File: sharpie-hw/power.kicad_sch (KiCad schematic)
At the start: 11 parts, among them J1 USB_C_Receptacle, U1 TLV1117-33, U2 TLV75801PDBV

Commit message: sharpie-hw prototype 1: complete
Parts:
- removed J1: USB_C_Receptacle, symbol Connector:USB_C_Receptacle
- removed U1: TLV1117-33, symbol Regulator_Linear:TLV1117-33
- removed U2: TLV75801PDBV, Package_TO_SOT_SMD:SOT-23-5, symbol Regulator_Linear:TLV75801PDBV
- added C22, C23: 100n, symbol Device:C
- added C24: 1u X7R, symbol Device:C
- added C25, C26: 10u X7R, symbol Device:C
- added J3: USB_C_Receptacle_USB2.0_16P, symbol Connector:USB_C_Receptacle_USB2.0_16P
- added J6: Conn_01x02_MountingPin, symbol Connector_Generic_MountingPin:Conn_01x02_MountingPin
- added R12: 100k, symbol Device:R
- added U1: TPS7A2533, symbol sharpie-hw:TPS7A2533
- added U2: TPS7A2501, symbol sharpie-hw:TPS7A2501
- added U5: LS021B7DD02, symbol sharpie-hw:Sharp_LS021B7DD02
- added U7: AP3602A, symbol sharpie-hw:AP3602A
- C2: value 2.2u X7R -> 1u X7R
- C3: value 1u X7R -> 2.2u X7R
- R3: value 62k -> 1.62M
- R4: value 13k -> 1.02M
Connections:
- net +3.2V: now also C23.1, U2.1 (OUT), U5.9 (VDD1)
- net +3.3V: now also U1.1 (OUT)
- net +5V: now also C22.1, C26.1, U5.1 (VDD2), U7.1 (Vout); no longer C1.1, C2.1
- net D+: now also J3.A6 (D+), J3.B6 (D+)
- net D-: now also J3.A7 (D-), J3.B7 (D-)
- net GND: now also C22.2, C23.2, C25.2, C26.2, J3.A1 (GND), J3.A12 (GND), J3.B1 (GND), J3.B12 (GND), J3.S1 (SHIELD), J6.1 (Pin_1), J6.MP (MountPin), R12.2, U1.3 (PG), U1.5 (GND), U2.3 (PG), U2.5 (GND), U5.10 (VSS), U7.2 (GND)
- net at R3.2, R4.1: now also U2.2 (FB)
- net at R1.1: now also J3.A5 (CC1)
- net at R2.1: now also J3.B5 (CC2)
- new net: C24.1, U7.4 (C+)
- new net: C24.2, U7.6 (C-)
- new net 5V EN: R12.1, U7.3 (~{SHDN})
- new net B0: U5.17 (B0)
- new net B1: U5.18 (B1)
- new net BCK: U5.12 (BCK)
- new net BSP: U5.11 (BSP)
- new net G0: U5.15 (G0)
- new net G1: U5.16 (G1)
- new net GCK: U5.4 (GCK)
- new net GEN: U5.5 (GEN)
- new net GSP: U5.3 (GSP)
- new net INTB: U5.6 (INTB)
- new net R0: U5.13 (R0)
- new net R1: U5.14 (R1)
- new net VA_VCOM: U5.20 (VCOM), U5.8 (VA)
- new net VB: U5.7 (VB)
- new net VCC: C1.1, C2.1, C25.1, J3.A4 (VBUS), J3.A9 (VBUS), J3.B4 (VBUS), J3.B9 (VBUS), J6.2 (Pin_2), U1.3 (PG), U1.6 (IN), U2.3 (PG), U2.6 (IN), U7.5 (Vin)
- no-connect marks 10 -> 2
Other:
- note added: "3.2V regulator"
- note added: "3.3V regulator"
- note added: "5V charge pump plus 5V enable"
- note added: "Battery"
- note added: "Display"
- note added: "EN must not be floating, and it needs to stay low until we turn it on."
- note added: "Following Adafruit 4694, 2.7" Sharp memory display, we use an AP3602 with a 1u flying cap for the 5V supply."
- note added: "Following Adafruit battery pinout: p1 = GND, p2 = VCC"
- note added: "For all regulators: place caps close to chips"
- note added: "Place caps close to display connector"
- note added: "Place flying cap as close to chip as possible"
- note added: "Sharp says that VDD2 (5V) should rise at least 1ms after 3.3V, so RP2350 controls 5V EN."
- note added: "USB-C"
- note added: "VCC is both VBUS from USB and VBAT from the battery. Don't attach both at the same time!"
- note added: "V_out = V_FB*(1 + R1/R2) 3.209 = 1.24*(1 + 1.62M/1.02M) 1% Rs, R1/R2 ideal for 3.2V = 1.66, actual = 1.588 R1+R2 for 3.2V = 3.3M, actual=2.64M regulator is 300 mA, which is more than enough (screen is negligable and RP2350 can sink/source up to 100 mA)"
- note added: "basic 5V/3A sink, from https://hackaday.com/2023/08/07/ all-about-usb-c-example-circuits/"
- note added: "part must be TPS2A2501DRVR 300 mA max"
- note added: "part must be TPS7A2533DRVR 300 mA max TI says connect EN to VIN and PG to GND if unused"
- note removed: "1A max"
- note removed: "V_out = V_FB*(1 + R1/R2) 3.173 = 0.55*(1 + 62k/13k) V_FB from datasheet, use 1% resistors regulator is 500 mA, which is more than enough (screen is negligable and RP2350 can sink/source up to 100 mA)"
- note removed: "ripped from https://hackaday.com/2023/08/07/ all-about-usb-c-example-circuits/"
- moved on the sheet: C1, R1, R2

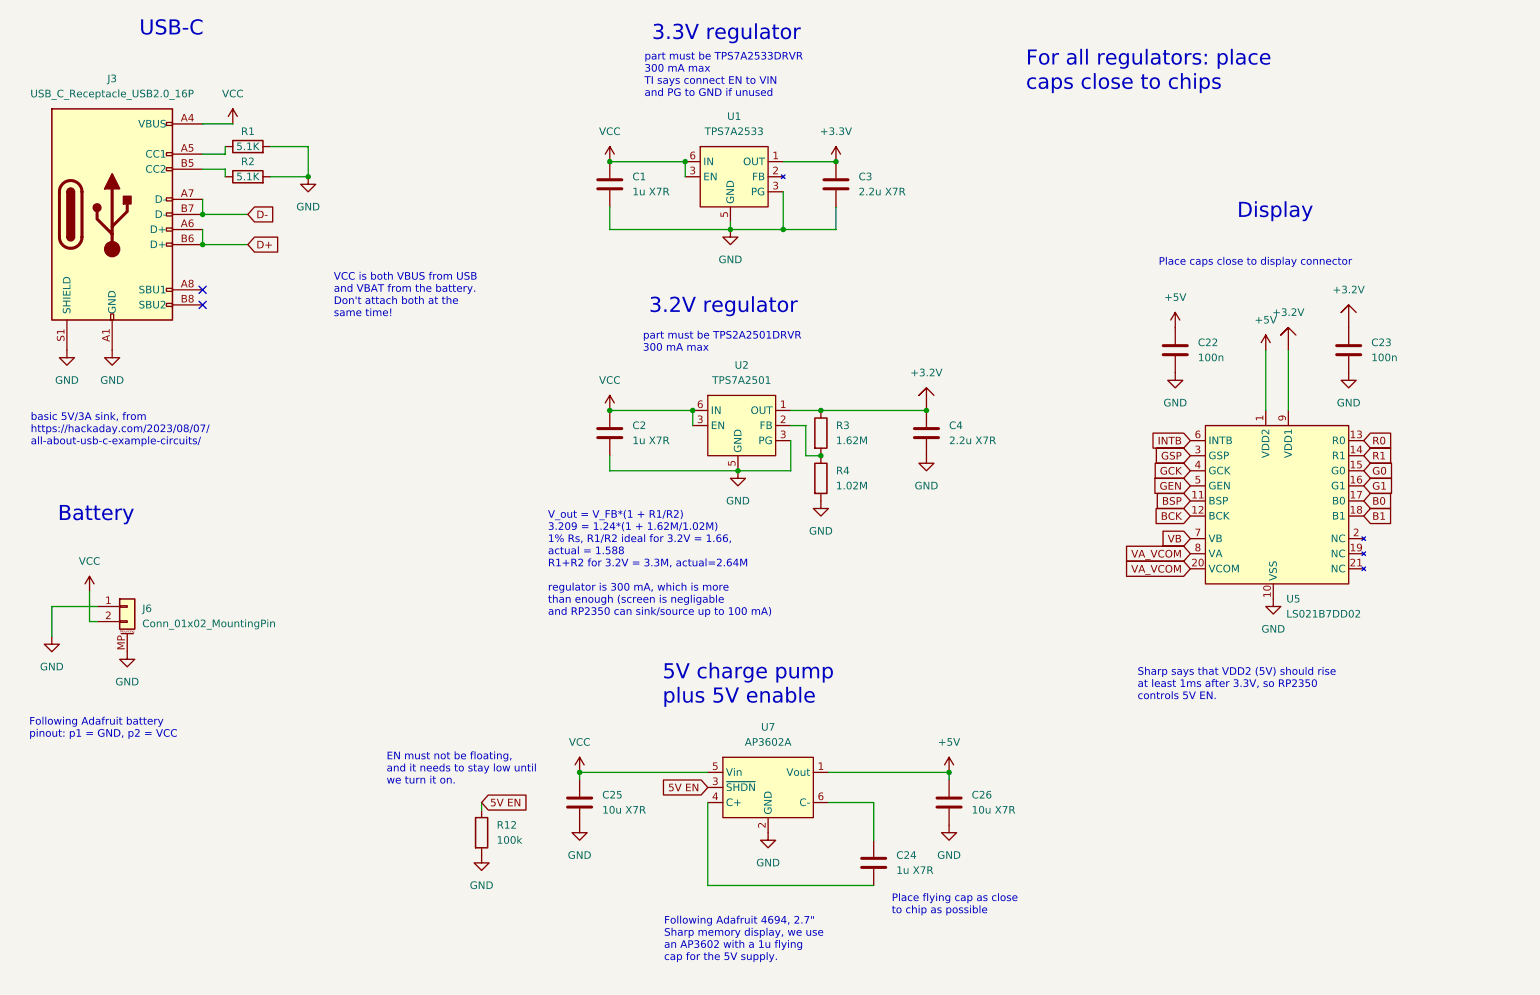
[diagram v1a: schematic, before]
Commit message: Finalize schematic, start PCB, configure manufacturing parameters, and start placing RP2350 components.
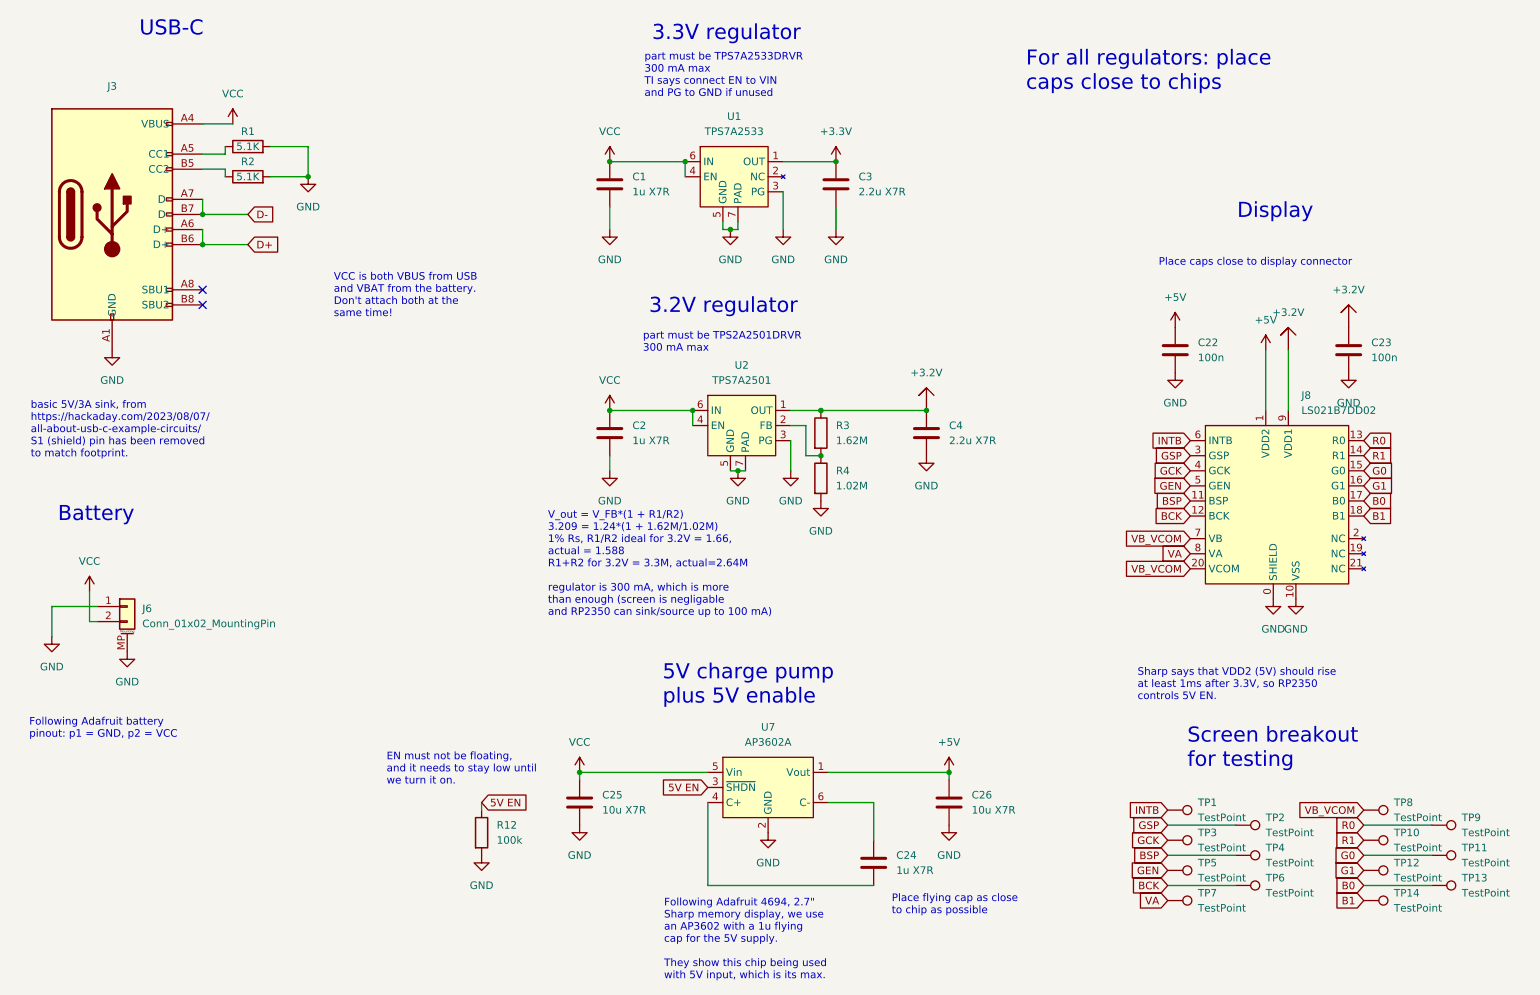
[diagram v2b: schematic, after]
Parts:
- removed J3: USB_C_Receptacle_USB2.0_16P, symbol Connector:USB_C_Receptacle_USB2.0_16P
- removed U5: LS021B7DD02, symbol sharpie-hw:Sharp_LS021B7DD02
- added J3: ~, Sharpie:USB-C_SMD-TYPE-C-31-M-12, symbol sharpie-hw:USB_C_Receptacle_USB2.0_16P_NoShield
- added J8: LS021B7DD02, Sharpie:FPC-SMD_21P-P0.30-503566-2102, symbol sharpie-hw:LS021B7DD02
- added TP1, TP10, TP11, TP12, TP13, TP14, TP2, TP3, TP4, TP5, TP6, TP7, TP8, TP9: TestPoint, TestPoint:TestPoint_Pad_D1.0mm, symbol Connector:TestPoint
- C1, C2, C24: footprint (none) -> Capacitor_SMD:C_0805_2012Metric; JLCPCB Part # (none) -> C519972
- C22, C23: footprint (none) -> Capacitor_SMD:C_0402_1005Metric; JLCPCB Part # (none) -> C49678
- C25, C26: footprint (none) -> Capacitor_SMD:C_0805_2012Metric; JLCPCB Part # (none) -> C527225
- C3, C4: footprint (none) -> Capacitor_SMD:C_0805_2012Metric; JLCPCB Part # (none) -> C520034
- J6: footprint (none) -> Connector_JST:JST_PH_S2B-PH-SM4-TB_1x02-1MP_P2.00mm_Horizontal; JLCPCB Part # (none) -> C295747
- R1, R2: footprint (none) -> Resistor_SMD:R_0402_1005Metric; JLCPCB Part # (none) -> C25905
- R12: footprint (none) -> Resistor_SMD:R_0402_1005Metric; JLCPCB Part # (none) -> C25530
- R3, R4: footprint (none) -> Resistor_SMD:R_0402_1005Metric; JLCPCB Part # (none) -> C166525
- U1: footprint (none) -> Package_SON:WSON-6-1EP_2x2mm_P0.65mm_EP1x1.6mm_ThermalVias; JLCPCB Part # (none) -> C2864326
- U2: footprint (none) -> Package_SON:WSON-6-1EP_2x2mm_P0.65mm_EP1x1.6mm_ThermalVias; JLCPCB Part # (none) -> C2867820
- U7: footprint (none) -> Package_TO_SOT_SMD:SOT-23-6; JLCPCB Part # (none) -> C460358
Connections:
- net +3.2V: now also J8.9 (VDD1)
- net +5V: now also J8.1 (VDD2)
- net B0: now also J8.17 (B0), TP13.1
- net B1: now also J8.18 (B1), TP14.1
- net BCK: now also J8.12 (BCK), TP6.1
- net BSP: now also J8.11 (BSP), TP4.1
- net D+: now also J3.A6 (D+), J3.B6 (D+)
- net D-: now also J3.A7 (D-), J3.B7 (D-)
- net G0: now also J8.15 (G0), TP11.1
- net G1: now also J8.16 (G1), TP12.1
- net GCK: now also J8.4 (GCK), TP3.1
- net GEN: now also J8.5 (GEN), TP5.1
- net GND: now also U1.7 (PAD), U2.7 (PAD), J3.A1 (GND), J3.A12 (GND), J3.B1 (GND), J3.B12 (GND), J8.0 (SHIELD), J8.10 (VSS)
- net GSP: now also J8.3 (GSP), TP2.1
- net INTB: now also J8.6 (INTB), TP1.1
- net R0: now also J8.13 (R0), TP9.1
- net R1: now also J8.14 (R1), TP10.1
- net VCC: now also U1.4 (EN), U2.4 (EN), J3.A4 (VBUS), J3.A9 (VBUS), J3.B4 (VBUS), J3.B9 (VBUS); no longer U1.3 (PG), U2.3 (PG)
- net at R1.1: now also J3.A5 (CC1)
- net at R2.1: now also J3.B5 (CC2)
- new net VA: J8.8 (VA), TP7.1
- new net VB_VCOM: J8.20 (VCOM), J8.7 (VB), TP8.1
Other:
- note added: "Following Adafruit 4694, 2.7" Sharp memory display, we use an AP3602 with a 1u flying cap for the 5V supply. They show this chip being used with 5V input, which is its max."
- note added: "Screen breakout for testing"
- note added: "basic 5V/3A sink, from https://hackaday.com/2023/08/07/ all-about-usb-c-example-circuits/ S1 (shield) pin has been removed to match footprint."
- note removed: "Following Adafruit 4694, 2.7" Sharp memory display, we use an AP3602 with a 1u flying cap for the 5V supply."
- note removed: "basic 5V/3A sink, from https://hackaday.com/2023/08/07/ all-about-usb-c-example-circuits/"

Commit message: Modify FPC footprint, add alternate USB-C footprint, and commit final (before review) design.
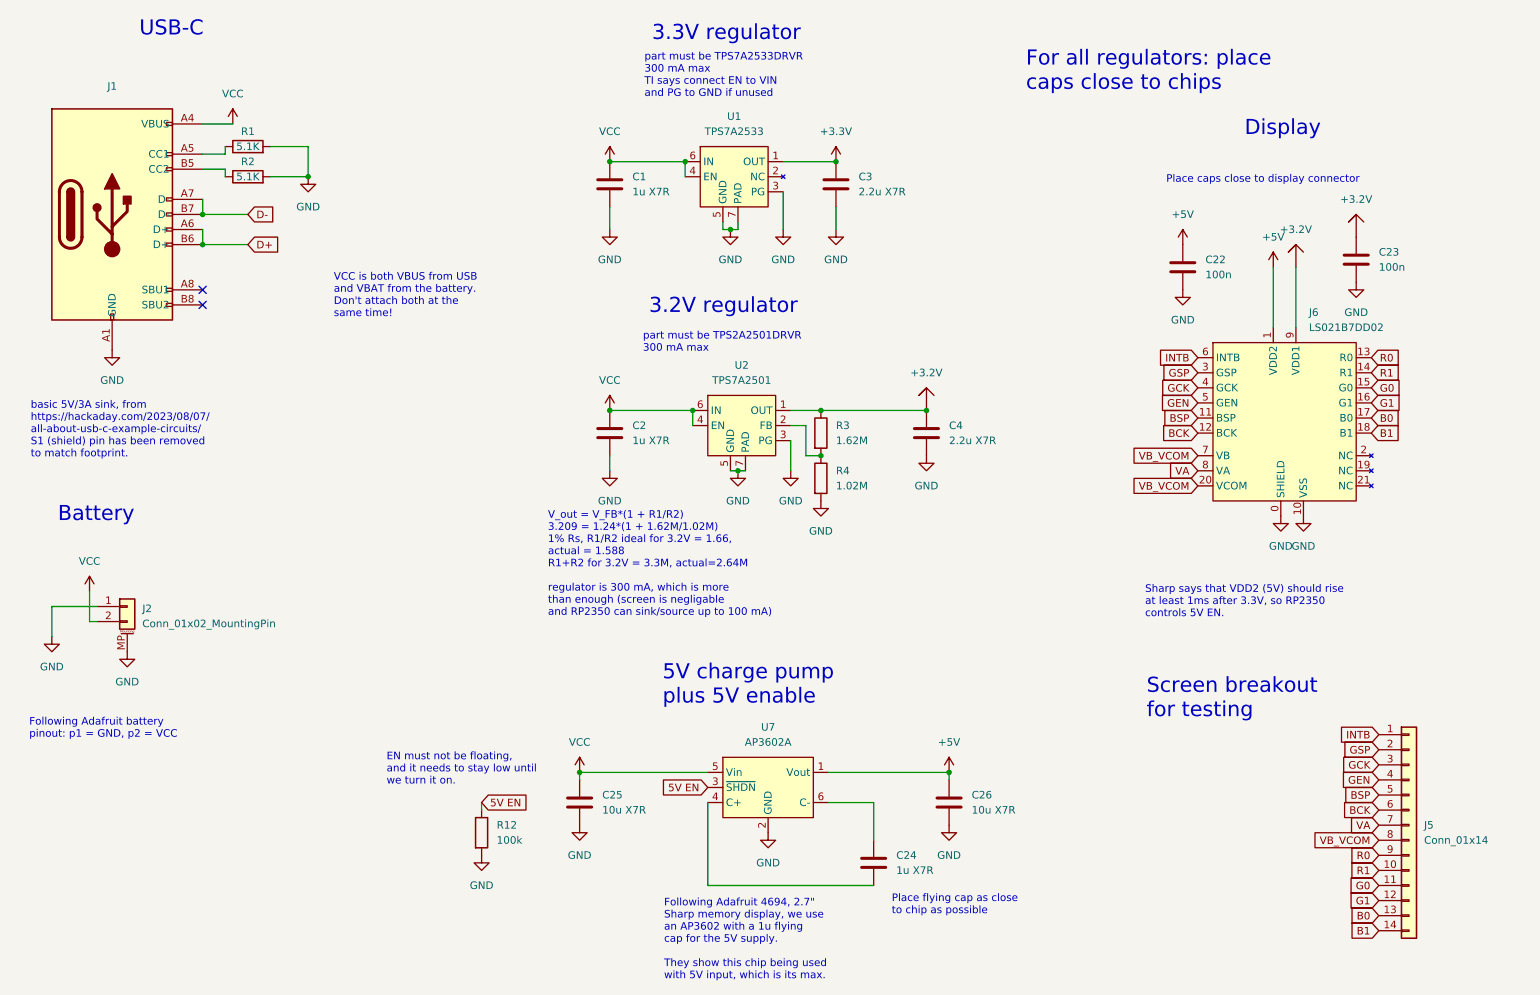
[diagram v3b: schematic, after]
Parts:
- removed TP1, TP10, TP11, TP12, TP13, TP14, TP2, TP3, TP4, TP5, TP6, TP7, TP8, TP9: TestPoint, TestPoint:TestPoint_Pad_D1.0mm, symbol Connector:TestPoint
- added J5: Conn_01x14, Connector_PinHeader_2.54mm:PinHeader_1x14_P2.54mm_Vertical, symbol Connector_Generic:Conn_01x14
- J1: renamed from J3; footprint Sharpie:USB-C_SMD-TYPE-C-31-M-12 -> Sharpie:TYPE-C-31-M-12
- renumbered J6 to J2, J8 to J6
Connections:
- net B0: now also J5.13 (Pin_13)
- net B1: now also J5.14 (Pin_14)
- net BCK: now also J5.6 (Pin_6)
- net BSP: now also J5.5 (Pin_5)
- net G0: now also J5.11 (Pin_11)
- net G1: now also J5.12 (Pin_12)
- net GCK: now also J5.3 (Pin_3)
- net GEN: now also J5.4 (Pin_4)
- net GSP: now also J5.2 (Pin_2)
- net INTB: now also J5.1 (Pin_1)
- net R0: now also J5.9 (Pin_9)
- net R1: now also J5.10 (Pin_10)
- net VA: now also J5.7 (Pin_7)
- net VB_VCOM: now also J5.8 (Pin_8)
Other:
- moved on the sheet: C22, C23, J6

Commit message: Add all JLCPCB part numbers and some PCB silkscreens.
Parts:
- C1, C2, C24: JLCPCB Part # C519972 -> C94122
- C22, C23: JLCPCB Part # C49678 -> C1525
- C25, C26: JLCPCB Part # C527225 -> C326595
- C3, C4: JLCPCB Part # C520034 -> C107128
- J1: JLCPCB Part # (none) -> C165948
- R4: JLCPCB Part # C166525 -> C26084
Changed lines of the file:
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@@
 			)
 		)
-		(property "JLCPCB Part #" "C520034"
+		(property "JLCPCB Part #" "C107128"
 			(at 170.18 85.09 0)
 			(effects
@@
 			)
 		)
-		(property "JLCPCB Part #" "C519972"
+		(property "JLCPCB Part #" "C94122"
 			(at 161.29 157.48 0)
 			(effects
@@
 			)
 		)
-		(property "JLCPCB Part #" "C520034"
+		(property "JLCPCB Part #" "C107128"
 			(at 154.94 43.18 0)
 			(effects
@@
 			)
 		)
-		(property "JLCPCB Part #" "C49678"
+		(property "JLCPCB Part #" "C1525"
 			(at 213.36 57.15 0)
 			(effects
@@
 			)
 		)
-		(property "JLCPCB Part #" "C166525"
+		(property "JLCPCB Part #" "C26084"
 			(at 152.4 92.71 0)
 			(effects
@@
 			)
 		)
+		(property "JLCPCB Part #" "C165948"
+			(at 33.02 49.53 0)
+			(effects
+				(font
+					(size 1.27 1.27)
+				)
+				(hide yes)
+			)
+		)
 		(pin "B12"
 		)
@@
 			)
 		)
-		(property "JLCPCB Part #" "C519972"
+		(property "JLCPCB Part #" "C94122"
 			(at 116.84 85.09 0)
 			(effects
@@
 			)
 		)
-		(property "JLCPCB Part #" "C527225"
+		(property "JLCPCB Part #" "C326595"
 			(at 111.76 147.32 0)
 			(effects
@@
 			)
 		)
-		(property "JLCPCB Part #" "C49678"
+		(property "JLCPCB Part #" "C1525"
 			(at 242.57 55.88 0)
 			(effects
@@
 			)
 		)
-		(property "JLCPCB Part #" "C527225"
+		(property "JLCPCB Part #" "C326595"
 			(at 173.99 147.32 0)
 			(effects
@@
 			)
 		)
-		(property "JLCPCB Part #" "C519972"
+		(property "JLCPCB Part #" "C94122"
 			(at 116.84 43.18 0)
 			(effects
